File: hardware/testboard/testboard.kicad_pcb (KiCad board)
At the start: 4 copper layers, 143 parts, among them J701 Barrel_Jack, J801 Conn_01x06, SW801 Button, SW901 Button, U201 68LC040, U202 74LVC1G04, U301 IS61C5128AS-25TLI, U302 IS61C5128AS-25TLI, U401 NB3N502, U501 MAX232, U502 68681, U503 MAX232, U701 AP2112K-3.3, U702 AP2112K-1.2, U801 SST26VF023BA, U802 SN74ALVC164245, U803 ICE40HX4K-TQ144, U804 SN74ALVC164245, U805 SN74ALVC164245, U806 SN74ALVC164245, U807 SN74ALVC164245, U808 SN74LVC07, U809 74AHCT04, U810 SN74LVC07, U901 TL7705A, U902 74LVC1G08, X401 ASE-33MHz, X402 33MHz, X403 33MHz, Y501 3.6864MHz

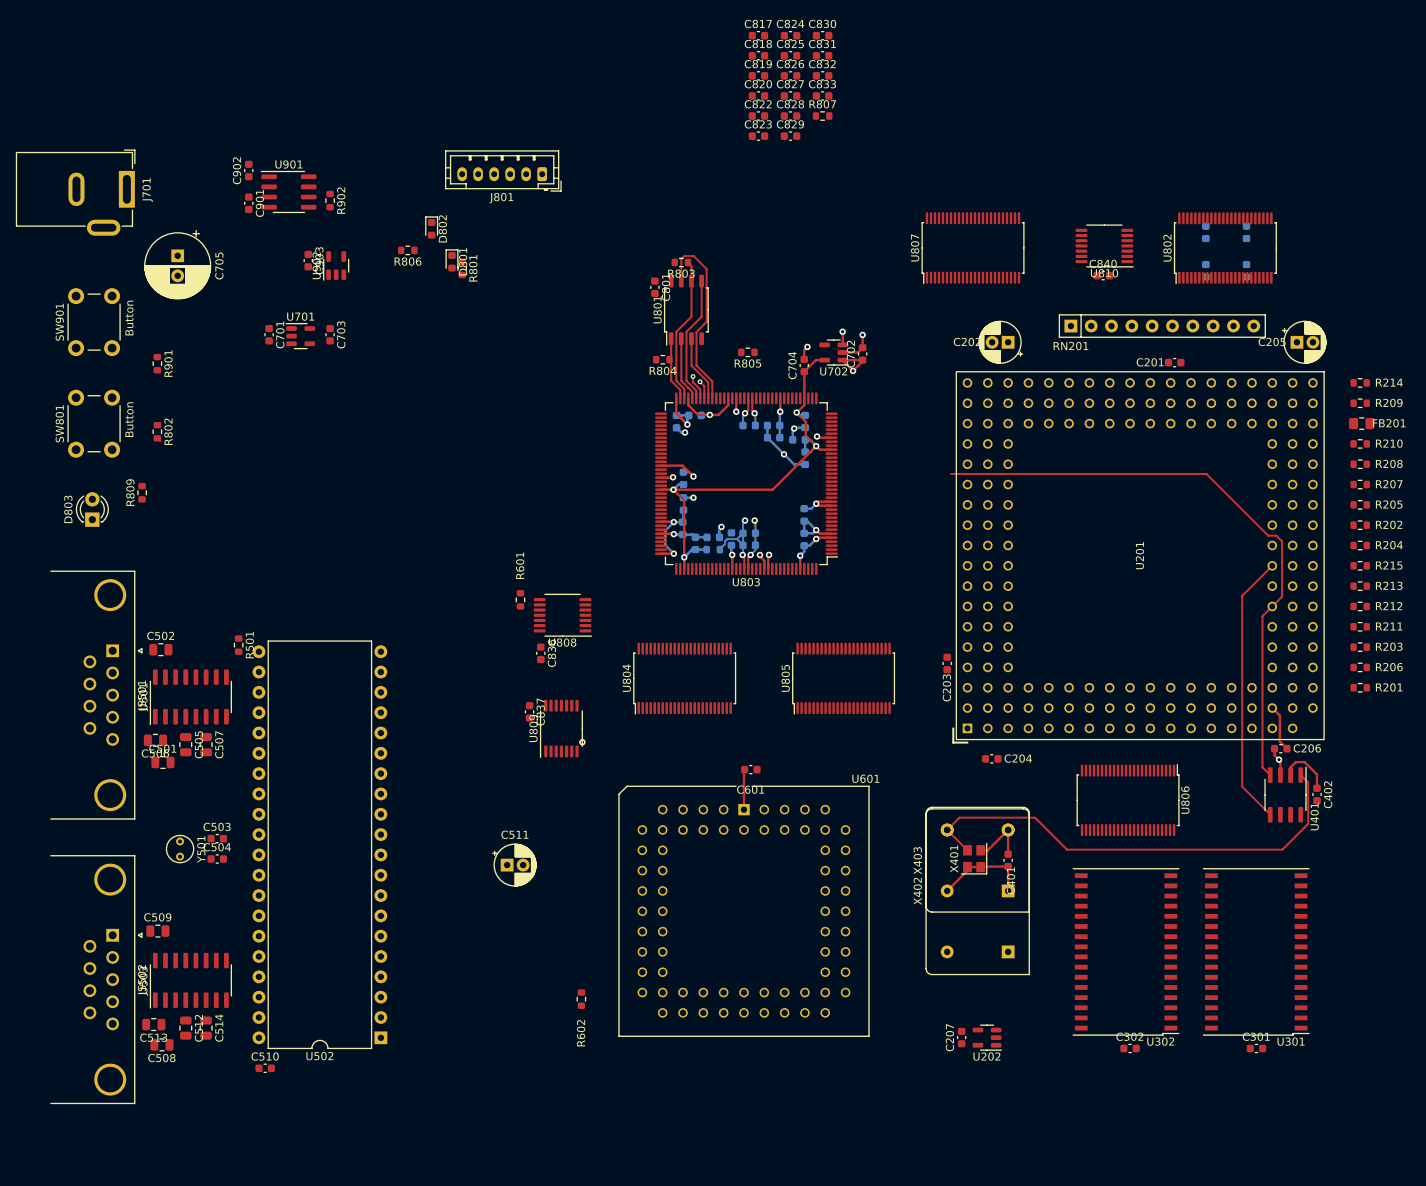
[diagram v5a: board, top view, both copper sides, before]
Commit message: testboard - schematic and route done
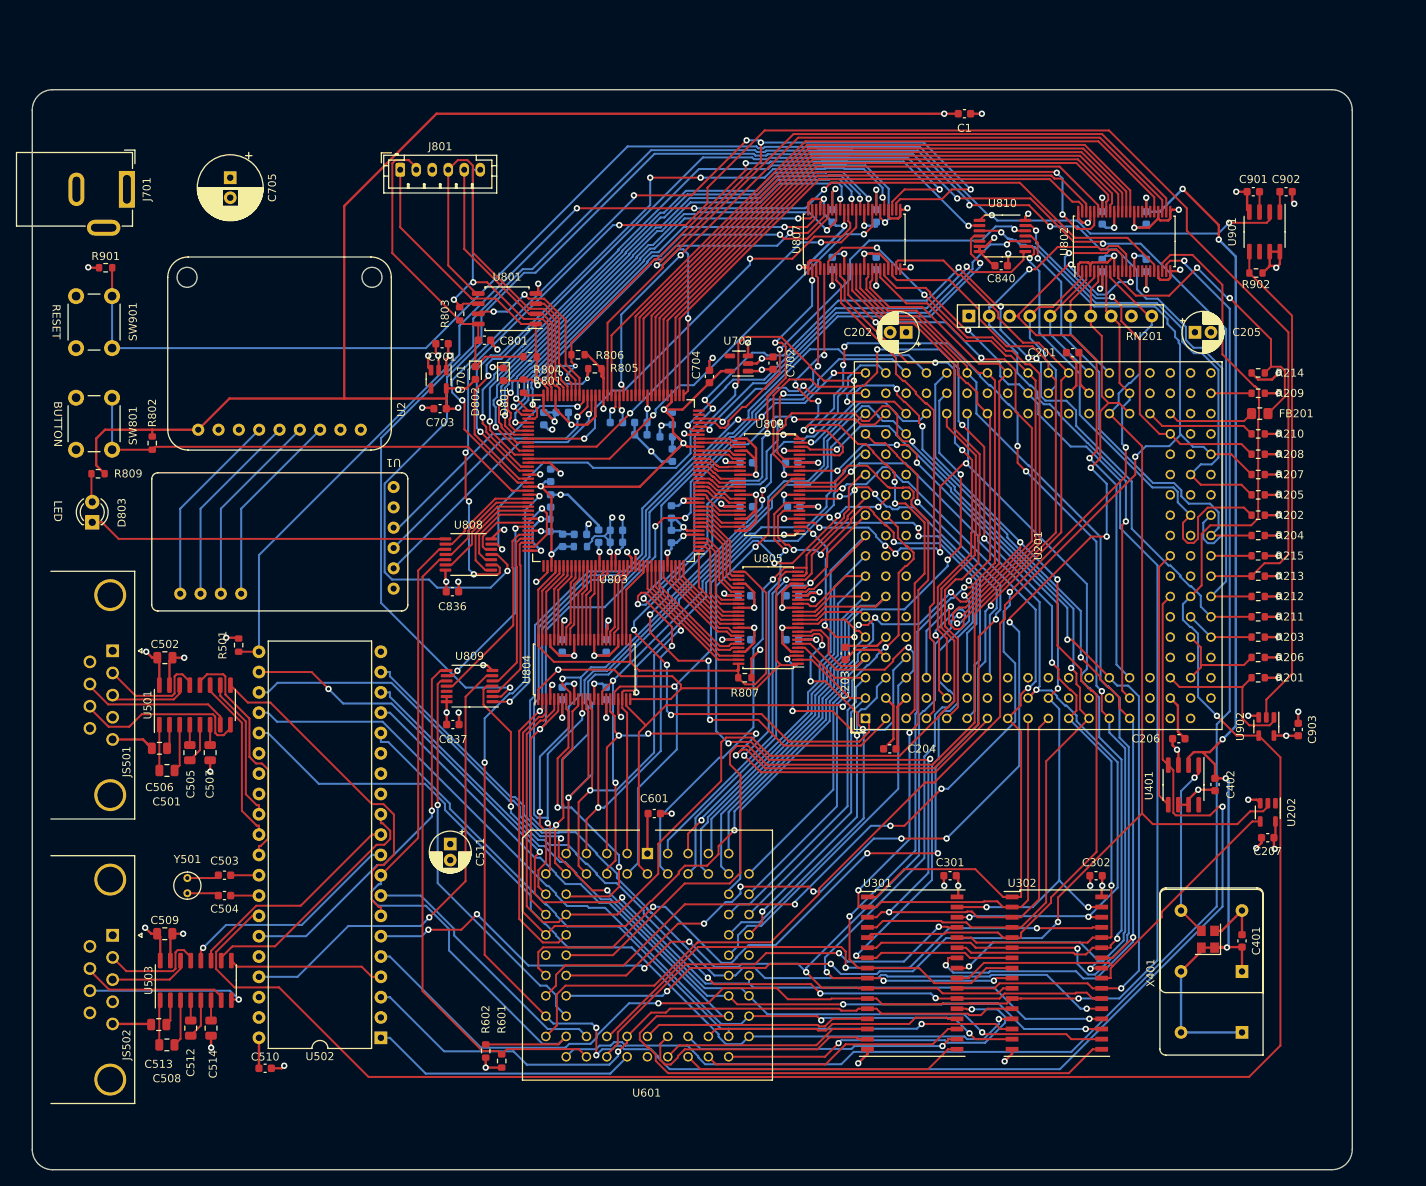
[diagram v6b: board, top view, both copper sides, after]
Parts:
- added C1: 4.7uF, Capacitor_SMD:C_0603_1608Metric, F.Cu at (141.5, 28.0)
- added U1: ~, 68040:DACMOD, F.Cu at (70.2, 74.7)
- added U2: MAX98306 Amp, 68040:AMP, F.Cu at (41.9, 67.5)
- C817, C818, C819, C820, C822, C823, C824, C825, C826, C827, C828, C829, C830, C831, C832, C833: moved to B.Cu
- SW801: value Button -> BUTTON
- SW901: value Button -> RESET
- moved C903 136.9 mm to (183.2, 105.0), turned to 90 degrees
- moved U902 129.8 mm to (179.3, 104.6), turned to -90 degrees
- moved C902 129.7 mm to (181.7, 37.8), turned to 0 degrees
- moved C901 125.6 mm to (177.6, 37.8), turned to 180 degrees
- moved U901 122.1 mm to (179.0, 42.8), turned to -90 degrees
- moved R902 116.1 mm to (178.0, 47.9), turned to 180 degrees
- moved C817 85.8 mm to (91.2, 100.5), turned to 90 degrees
- moved C830 80.9 mm to (96.8, 94.5), turned to -90 degrees
- moved C826 76.8 mm to (91.2, 94.5), turned to -90 degrees
- moved C822 74.7 mm to (96.8, 100.5), turned to 90 degrees
- moved C831 73.6 mm to (114.0, 93.8)
- moved C818 73.1 mm to (120.0, 93.8), turned to 180 degrees
- moved R807 70.9 mm to (114.1, 98.5), turned to 180 degrees
- moved C827 62.7 mm to (114.0, 88.2)
- moved U806 59.7 mm to (117.2, 74.4), turned to 180 degrees
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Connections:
- net /~{FPGA_RDY} renamed /~{FPGA_WAIT}
- U802 pad 16: /~{COM_IRQ} -> unconnected-(U802A-2B3-Pad16)
- U802 pad 19: /~{RST} -> unconnected-(U802A-2B5-Pad19)
- U802 pad 20: unconnected-(U802A-2B6-Pad20) -> /~{COM_IRQ}
- U802 pad 22: unconnected-(U802A-2B7-Pad22) -> /~{RST}
- U802 pad 27: unconnected-(U802A-2A7-Pad27) -> /FPGA/LV_~{RST}
- U802 pad 29: unconnected-(U802A-2A6-Pad29) -> /FPGA/LV_~{COM_IRQ}
- U802 pad 30: /FPGA/LV_~{RST} -> unconnected-(U802A-2A5-Pad30)
- U802 pad 33: /FPGA/LV_~{COM_IRQ} -> unconnected-(U802A-2A3-Pad33)
- U803 pad 1: /FPGA/LV_D6 -> /FPGA/LV_D9
- U803 pad 10: /FPGA/LV.A10 -> /FPGA/LV.A8
- U803 pad 101: /FPGA/LV_~{DSACK0} -> /FPGA/LV_~{IPL2}
- U803 pad 102: /FPGA/LV_~{DSACK1} -> /FPGA/LV_COM_CS
- U803 pad 104: /FPGA/LV_~{TA} -> /FPGA/LV_68150_CS
- U803 pad 105: /FPGA/LV_~{IPL0} -> /FPGA/LV_COM_IACK
- U803 pad 106: /FPGA/LV_~{IPL1} -> /FPGA/LV_RAM_CS
- U803 pad 107: /FPGA/LV_~{IPL2} -> /FPGA/LV_AVEC
- U803 pad 11: /FPGA/LV.A11 -> /FPGA/LV.A9
- U803 pad 12: /FPGA/LV.A12 -> /FPGA/LV.A21
- U803 pad 135: /FPGA/LV_D15 -> /FPGA/LV_D3
- U803 pad 136: /FPGA/LV_D14 -> /FPGA/LV_D1
- U803 pad 137: /FPGA/LV_D13 -> /FPGA/LV_D4
- U803 pad 138: /FPGA/LV_D12 -> /FPGA/LV_D0
- U803 pad 139: /FPGA/LV_D11 -> /FPGA/LV_D2
- U803 pad 141: /FPGA/LV_D10 -> /FPGA/LV_D5
- U803 pad 142: /FPGA/LV_D9 -> /FPGA/LV_D6
- U803 pad 143: /FPGA/LV_D8 -> /FPGA/LV_D7
- U803 pad 144: /FPGA/LV_D7 -> /FPGA/LV_D8
- U803 pad 15: /FPGA/LV.A13 -> /FPGA/LV.A25
- U803 pad 16: /FPGA/LV.A14 -> /FPGA/LV.A20
- U803 pad 17: /FPGA/LV.A16 -> /FPGA/LV.A23
- U803 pad 18: /FPGA/LV.A15 -> /FPGA/LV.A18
- U803 pad 19: /FPGA/LV.A17 -> /FPGA/LV.A19
- U803 pad 2: /FPGA/LV_D5 -> /FPGA/LV_D10
- U803 pad 20: /BCLK -> unconnected-(U803D-IOL_13B_GBIN7-Pad20)
- U803 pad 21: /FPGA/LV.A19 -> /FPGA/LV.A17
- U803 pad 22: /FPGA/LV.A18 -> /FPGA/LV.A15
- U803 pad 23: /FPGA/LV.A23 -> /FPGA/LV.A16
- U803 pad 24: /FPGA/LV.A20 -> /FPGA/LV.A14
- U803 pad 25: /FPGA/LV.A25 -> /FPGA/LV.A13
- U803 pad 26: /FPGA/LV.A21 -> /FPGA/LV.A12
- U803 pad 28: /FPGA/LV.A9 -> /FPGA/LV.A11
- U803 pad 29: /FPGA/LV.A8 -> /FPGA/LV.A10
- U803 pad 3: /FPGA/LV_D4 -> /FPGA/LV_D11
- U803 pad 31: unconnected-(U803D-IOL_24A-Pad31) -> /FPGA/LV_~{TBI}
- U803 pad 32: unconnected-(U803D-IOL_24B-Pad32) -> /FPGA/LV_~{TCI}
- U803 pad 33: unconnected-(U803D-IOL_25A-Pad33) -> /FPGA/LV_~{TEA}
- U803 pad 34: unconnected-(U803D-IOL_25B-Pad34) -> /FPGA/LV_~{TA}
- U803 pad 38: unconnected-(U803C-IOB_57-Pad38) -> /FPGA/LV_TM2
- U803 pad 39: /FPGA/LV_COM_IACK -> /FPGA/LV_TM1
- U803 pad 4: /FPGA/LV_D3 -> /FPGA/LV_D12
- U803 pad 41: /FPGA/LV_RAM_CS -> /FPGA/LV_TM0
- U803 pad 42: /FPGA/LV_AVEC -> /FPGA/LV_R/~{W}
- U803 pad 43: /FPGA/LV_COM_CS -> /FPGA/LV_SIZ0
- U803 pad 44: /FPGA/LV_68150_CS -> /FPGA/LV_SIZ1
- U803 pad 45: unconnected-(U803C-IOB_73-Pad45) -> /FPGA/LV_~{TS}
- U803 pad 47: unconnected-(U803C-IOB_79-Pad47) -> /FPGA/LV_~{TIP}
- U803 pad 48: /FPGA/LV_~{RST} -> /FPGA/LV_TT1
- U803 pad 49: unconnected-(U803C-IOB_81_GBIN5-Pad49) -> /FPGA/LV_TT0
- U803 pad 52: /FPGA/FPGA_LED -> /FPGA/LV_~{RST}
- U803 pad 55: /FPGA/FPGA_BTN -> /FPGA/LV_~{COM_IRQ}
- U803 pad 56: unconnected-(U803C-IOB_94-Pad56) -> /FPGA/LV_~{68150_DS}
- U803 pad 60: unconnected-(U803C-IOB_95-Pad60) -> /FPGA/SND_BCLK
- U803 pad 61: unconnected-(U803C-IOB_96-Pad61) -> /FPGA/SND_DOUT
- U803 pad 62: unconnected-(U803C-IOB_102-Pad62) -> /FPGA/SND_LRCLK
- U803 pad 7: /FPGA/LV_D2 -> /FPGA/LV_D13
- U803 pad 8: /FPGA/LV_D1 -> /FPGA/LV_D14
- U803 pad 9: /FPGA/LV_D0 -> /FPGA/LV_D15
- U803 pad 93: unconnected-(U803B-IOR_140_GBIN3-Pad93) -> /FPGA/FPGA_BTN
- U803 pad 94: unconnected-(U803B-IOR_141_GBIN2-Pad94) -> /BCLK
- U803 pad 95: unconnected-(U803B-IOR_144-Pad95) -> /FPGA/FPGA_LED
- U803 pad 96: unconnected-(U803B-IOR_146-Pad96) -> /FPGA/LV_~{DSACK0}
- U803 pad 97: unconnected-(U803B-IOR_147-Pad97) -> /FPGA/LV_~{DSACK1}
- U803 pad 98: unconnected-(U803B-IOR_148-Pad98) -> /FPGA/LV_~{IPL0}
- U803 pad 99: unconnected-(U803B-IOR_152-Pad99) -> /FPGA/LV_~{IPL1}
- U805 pad 11: /D9 -> /D6
- U805 pad 12: /D8 -> /D7
- U805 pad 13: /D7 -> /D8
- U805 pad 14: /D6 -> /D9
- U805 pad 16: /D5 -> /D10
- U805 pad 17: /D4 -> /D11
- U805 pad 19: /D3 -> /D12
- U805 pad 2: /D15 -> /D3
- U805 pad 20: /D2 -> /D13
- U805 pad 22: /D1 -> /D14
- U805 pad 23: /D0 -> /D15
- U805 pad 26: /FPGA/LV_D0 -> /FPGA/LV_D15
- U805 pad 27: /FPGA/LV_D1 -> /FPGA/LV_D14
- U805 pad 29: /FPGA/LV_D2 -> /FPGA/LV_D13
- U805 pad 3: /D14 -> /D1
- U805 pad 30: /FPGA/LV_D3 -> /FPGA/LV_D12
- U805 pad 32: /FPGA/LV_D4 -> /FPGA/LV_D11
- U805 pad 33: /FPGA/LV_D5 -> /FPGA/LV_D10
- U805 pad 35: /FPGA/LV_D6 -> /FPGA/LV_D9
- U805 pad 36: /FPGA/LV_D7 -> /FPGA/LV_D8
- U805 pad 37: /FPGA/LV_D8 -> /FPGA/LV_D7
- U805 pad 38: /FPGA/LV_D9 -> /FPGA/LV_D6
- U805 pad 40: /FPGA/LV_D10 -> /FPGA/LV_D5
- U805 pad 41: /FPGA/LV_D11 -> /FPGA/LV_D2
- U805 pad 43: /FPGA/LV_D12 -> /FPGA/LV_D0
- U805 pad 44: /FPGA/LV_D13 -> /FPGA/LV_D4
- U805 pad 46: /FPGA/LV_D14 -> /FPGA/LV_D1
- U805 pad 47: /FPGA/LV_D15 -> /FPGA/LV_D3
- U805 pad 5: /D13 -> /D4
- U805 pad 6: /D12 -> /D0
- U805 pad 8: /D11 -> /D2
- U805 pad 9: /D10 -> /D5
- U806 pad 11: /A15 -> /A18
- U806 pad 12: /A17 -> /A19
- U806 pad 13: /A19 -> /A17
- U806 pad 14: /A18 -> /A15
- U806 pad 16: /A23 -> /A16
- U806 pad 17: /A20 -> /A14
- U806 pad 19: /A25 -> /A13
- U806 pad 2: /A10 -> /A8
- U806 pad 20: /A21 -> /A12
- U806 pad 22: /A9 -> /A11
- U806 pad 23: /A8 -> /A10
- U806 pad 26: /FPGA/LV.A8 -> /FPGA/LV.A10
- U806 pad 27: /FPGA/LV.A9 -> /FPGA/LV.A11
- U806 pad 29: /FPGA/LV.A21 -> /FPGA/LV.A12
- U806 pad 3: /A11 -> /A9
- U806 pad 30: /FPGA/LV.A25 -> /FPGA/LV.A13
- U806 pad 32: /FPGA/LV.A20 -> /FPGA/LV.A14
- U806 pad 33: /FPGA/LV.A23 -> /FPGA/LV.A16
- U806 pad 35: /FPGA/LV.A18 -> /FPGA/LV.A15
- U806 pad 36: /FPGA/LV.A19 -> /FPGA/LV.A17
- U806 pad 37: /FPGA/LV.A17 -> /FPGA/LV.A19
- U806 pad 38: /FPGA/LV.A15 -> /FPGA/LV.A18
- U806 pad 40: /FPGA/LV.A16 -> /FPGA/LV.A23
- U806 pad 41: /FPGA/LV.A14 -> /FPGA/LV.A20
- U806 pad 43: /FPGA/LV.A13 -> /FPGA/LV.A25
- U806 pad 44: /FPGA/LV.A12 -> /FPGA/LV.A21
- U806 pad 46: /FPGA/LV.A11 -> /FPGA/LV.A9
- U806 pad 47: /FPGA/LV.A10 -> /FPGA/LV.A8
- U806 pad 5: /A12 -> /A21
- U806 pad 6: /A13 -> /A25
- U806 pad 8: /A14 -> /A20
- U806 pad 9: /A16 -> /A23
- U808 pad 10: /~{DSACK1} -> /~{DSACK0}
- U808 pad 11: /FPGA/LV_~{DSACK1} -> /FPGA/LV_~{DSACK0}
- U808 pad 12: /~{TA} -> /~{DSACK1}
- U808 pad 13: /FPGA/LV_~{TA} -> /FPGA/LV_~{DSACK1}
- U808 pad 8: /~{DSACK0} -> Net-(D803-K)
- U808 pad 9: /FPGA/LV_~{DSACK0} -> /FPGA/FPGA_LED
- U810 pad 10: Net-(D803-K) -> /~{TA}
- U810 pad 11: /FPGA/FPGA_LED -> /FPGA/LV_~{TA}
- U810 pad 13: unconnected-(U810-Pad13) -> +3.3V
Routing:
- net +3.3V: track 61.9 -> 415.7 mm, vias 11 -> 32
- net GND: track 65.7 -> 352.3 mm, vias 15 -> 76
- net /~{RST}: track 0.00 -> 270.8 mm, vias 0 -> 1
- net /A2: track 0.00 -> 213.0 mm, vias 0 -> 3
- net /~{IPL1}: track 0.00 -> 207.4 mm, vias 0 -> 3
- net /~{AVEC}: track 0.00 -> 207.1 mm, vias 0 -> 3
- net /A3: track 0.00 -> 199.6 mm, vias 0 -> 6
- net /~{IPL0}: track 0.00 -> 198.0 mm, vias 0 -> 4
- net /~{DS}: track 0.00 -> 178.5 mm, vias 0 -> 1
- net /~{TA}: track 0.00 -> 176.5 mm, vias 0 -> 2
- net /R/~{W}: track 0.00 -> 176.0 mm, vias 0 -> 3
- net /~{FPGA_WAIT}: track 0.00 -> 173.4 mm, vias 0 -> 2
- net /A0: track 0.00 -> 160.0 mm, vias 0 -> 4
- net /~{COM_IRQ}: track 0.00 -> 153.0 mm, vias 0 -> 3
- net /FPGA/LV.A0: track 0.00 -> 152.1 mm, vias 0 -> 7
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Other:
- board outline added: 165 x 135 mm

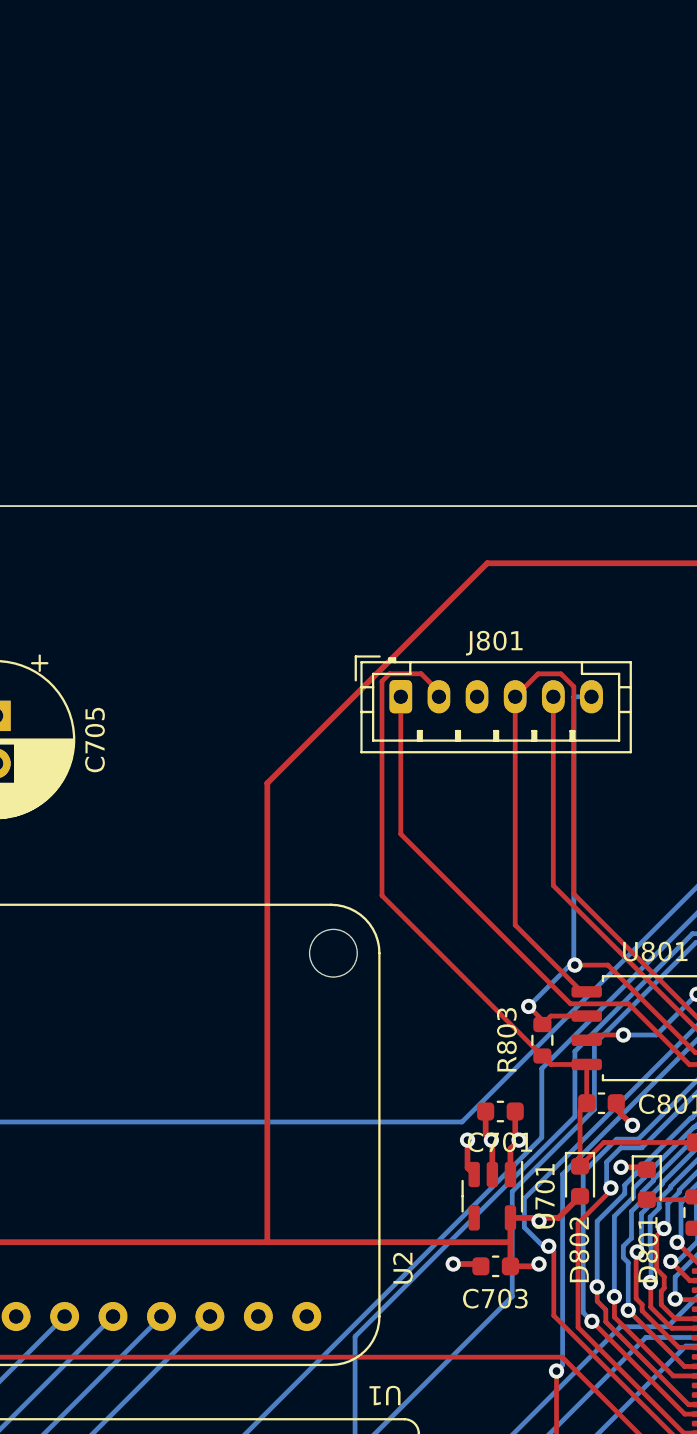
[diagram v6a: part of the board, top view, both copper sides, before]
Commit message: make 3.3v reg bigger
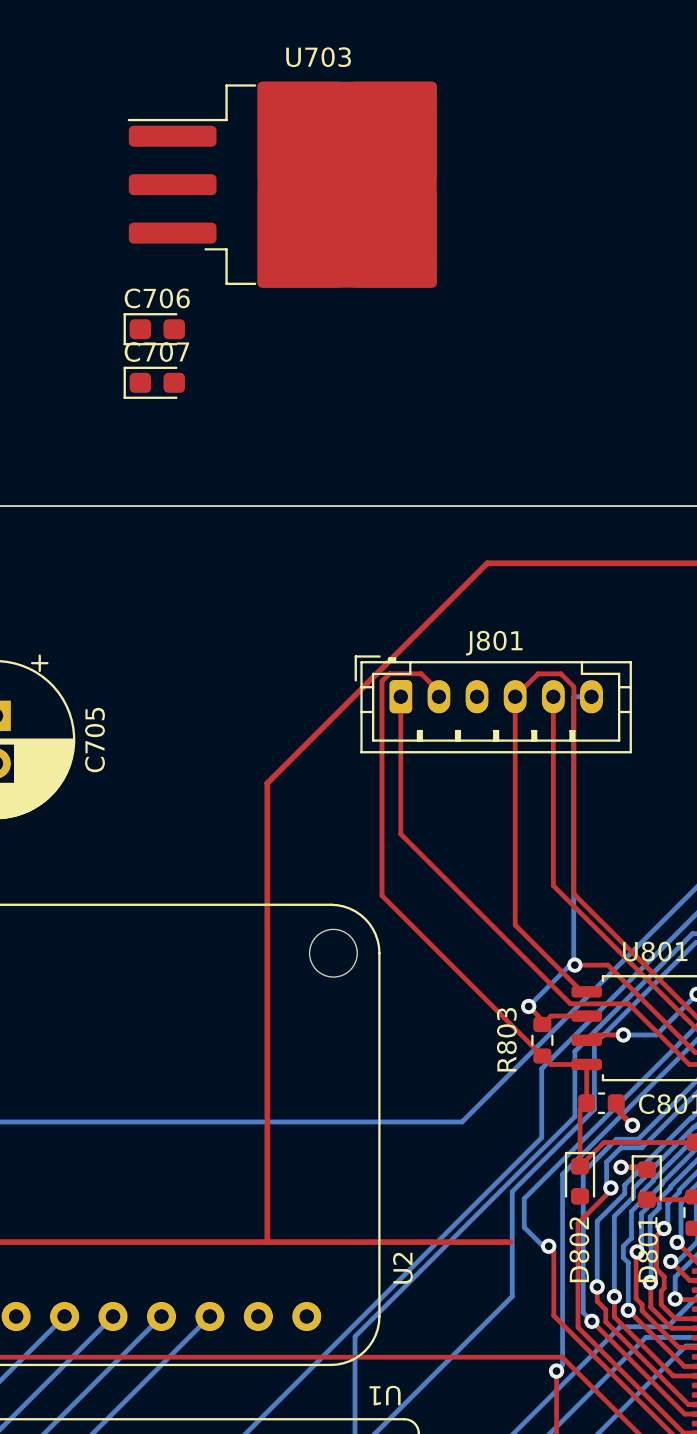
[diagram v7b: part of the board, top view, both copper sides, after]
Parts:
- removed C701, C703: 4.7uF, Capacitor_SMD:C_0603_1608Metric
- removed U701: AP2112K-3.3, Package_TO_SOT_SMD:SOT-23-5
- added C706: 22uF, Capacitor_Tantalum_SMD:CP_EIA-2012-12_Kemet-R, F.Cu at (58.2, 15.7)
- added C707: 10uF, Capacitor_Tantalum_SMD:CP_EIA-2012-12_Kemet-R, F.Cu at (58.2, 18.5)
- added U703: LT1084-3.3, Package_TO_SOT_SMD:TO-263-3_TabPin2, F.Cu at (66.7, 8.15)
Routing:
- net +3.3V: track 415.7 -> 407.3 mm, vias 32 -> 30
- net +5V: track 159.8 -> 154.3 mm, vias 40 -> 38
- net GND: track 352.3 -> 347.3 mm, vias 76 -> 74
